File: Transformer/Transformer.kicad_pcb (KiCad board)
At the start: 4 copper layers, 36 x 30 mm, 0 parts

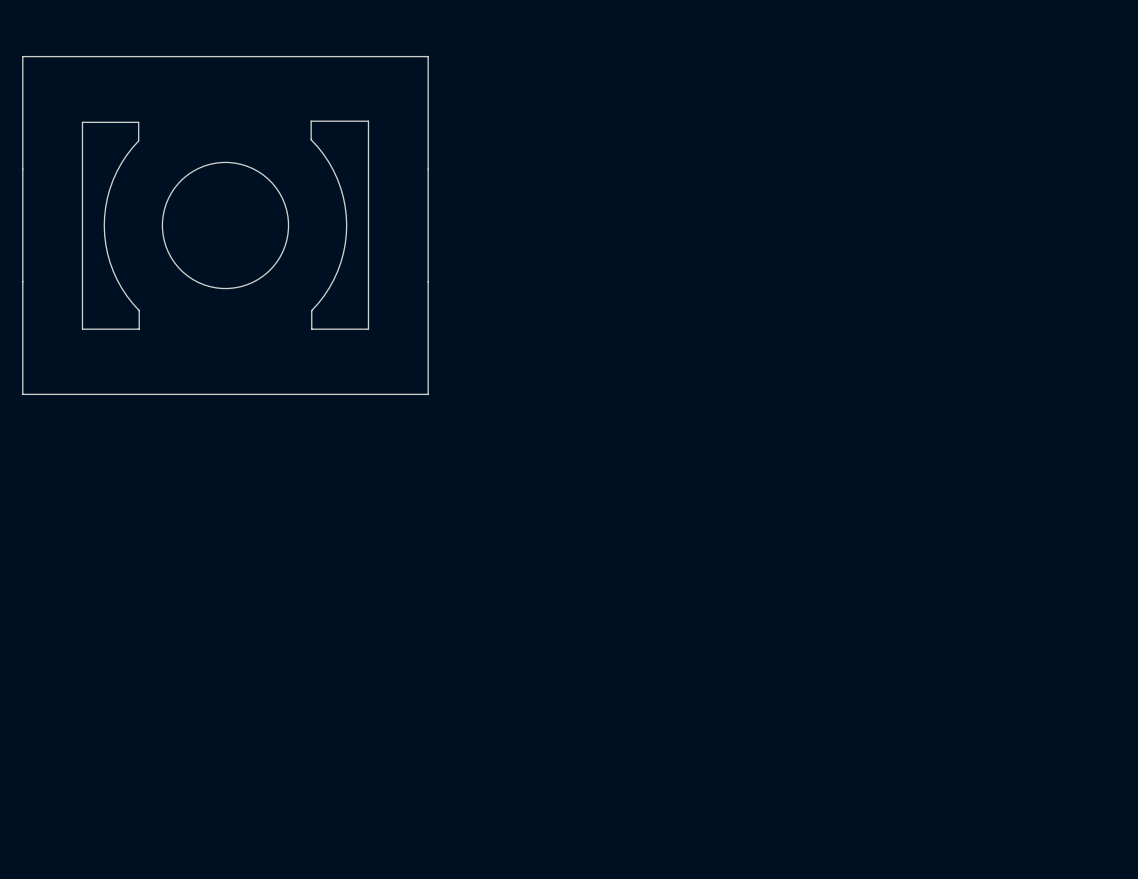
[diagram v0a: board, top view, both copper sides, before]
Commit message: Updated transformer
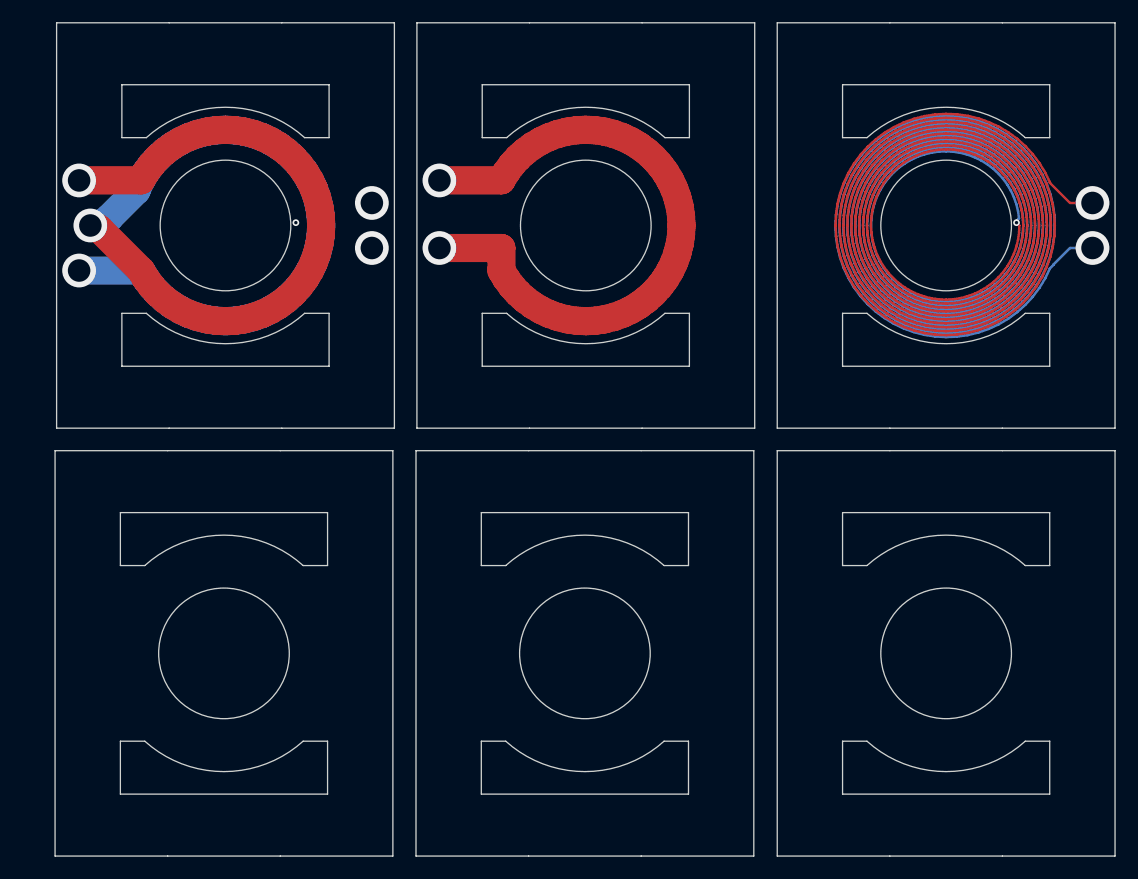
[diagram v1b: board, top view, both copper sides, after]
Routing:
- net (no net): track 0.00 -> 2247.1 mm, vias 0 -> 11
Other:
- board size 36 x 30 mm -> 94.1 x 74 mm

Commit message: Finished transformer
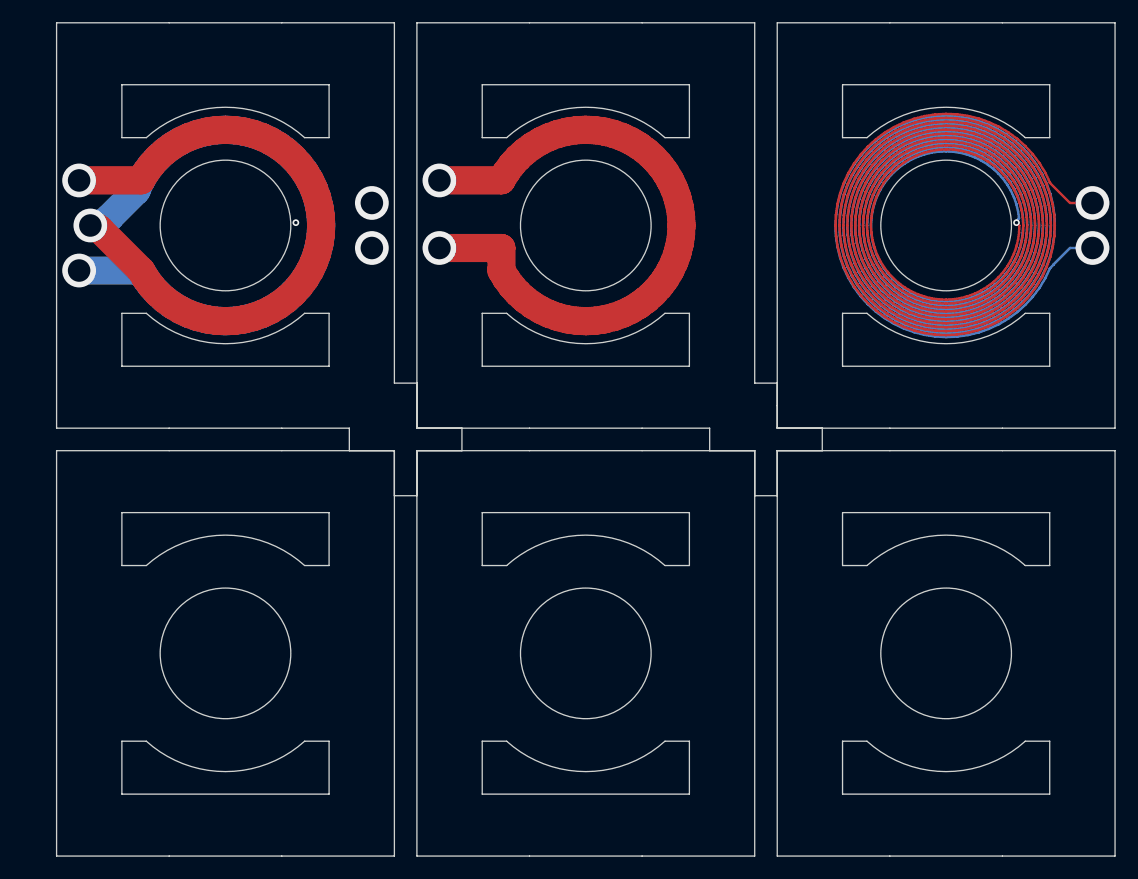
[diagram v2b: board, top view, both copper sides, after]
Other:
- board size 94.1 x 74 mm -> 94 x 74 mm

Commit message: Added vias to transformer blanks
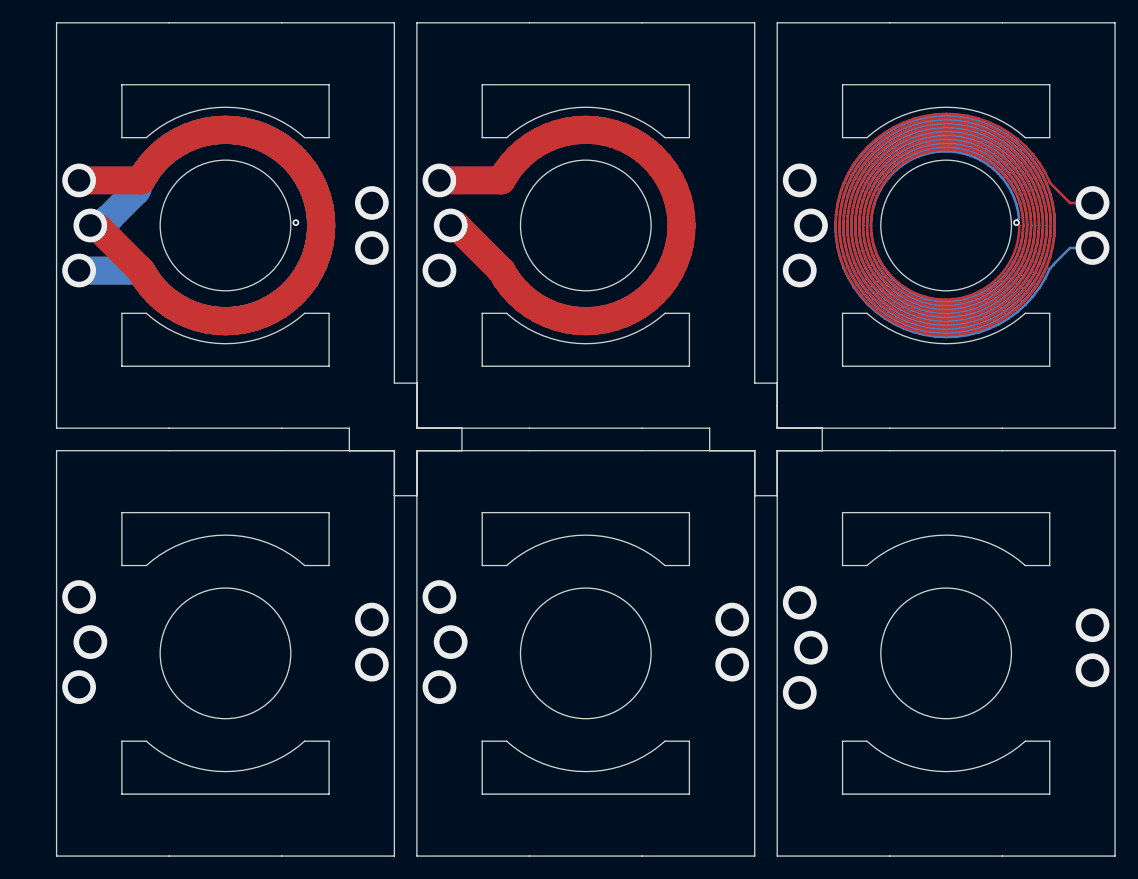
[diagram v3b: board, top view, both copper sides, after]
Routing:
- net (no net): track 2247.1 -> 2245.8 mm, vias 11 -> 30
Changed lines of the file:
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@@
 	)
 	(segment
+		(start 80.496797 63)
+		(end 80 63)
+		(width 2.5)
+		(layer "F.Cu")
+		(net "")
+	)
+	(segment
 		(start 129.931081 70.227043)
 		(end 129.197185 70.778138)
@@
 	)
 	(segment
+		(start 84.503669 67.006872)
+		(end 80.496797 63)
+		(width 2.5)
+		(layer "F.Cu")
+		(net "")
+	)
+	(segment
 		(start 130.297669 56.70233)
 		(end 130.888851 57.346465)
@@
 	)
 	(segment
-		(start 84.487076 65)
-		(end 79 65)
-		(width 2.5)
-		(layer "F.Cu")
-		(net "")
-	)
-	(segment
 		(start 117.828618 66.298672)
 		(end 117.529956 65.679979)
@@
 	)
 	(segment
-		(start 84.503669 65.016593)
-		(end 84.487076 65)
-		(width 2.5)
-		(layer "F.Cu")
-		(net "")
-	)
-	(segment
 		(start 117.628123 64.932887)
 		(end 117.463985 64.300094)
@@
 	)
 	(segment
-		(start 84.503669 67.006872)
-		(end 84.503669 65.016593)
-		(width 2.5)
-		(layer "F.Cu")
-		(net "")
-	)
-	(segment
 		(start 131.86908 58.793888)
 		(end 132.248511 59.583354)
@@
 	)
 	(via
+		(at 111 104.5)
+		(size 3)
+		(drill 2)
+		(layers "F.Cu" "B.Cu")
+		(net "")
+	)
+	(via
 		(at 137 61)
 		(size 3)
@@
 	)
 	(via
+		(at 137 98.5)
+		(size 3)
+		(drill 2)
+		(layers "F.Cu" "B.Cu")
+		(net "")
+	)
+	(via
+		(at 73 102)
+		(size 3)
+		(drill 2)
+		(layers "F.Cu" "B.Cu")
+		(net "")
+	)
+	(via
 		(at 79 59)
 		(size 3)
@@
 	)
 	(via
-		(at 79 65)
+		(at 105 98)
+		(size 3)
+		(drill 2)
+		(layers "F.Cu" "B.Cu")
+		(net "")
+	)
+	(via
+		(at 112 100.5)
+		(size 3)
+		(drill 2)
+		(layers "F.Cu" "B.Cu")
+		(net "")
+	)
+	(via
+		(at 80 63)
 		(size 3)
 		(drill 2)
@@
 	)
 	(via
+		(at 48 100)
+		(size 3)
+		(drill 2)
+		(layers "F.Cu" "B.Cu")
+		(net "")
+	)
+	(via
+		(at 111 96.5)
+		(size 3)
+		(drill 2)
+		(layers "F.Cu" "B.Cu")
+		(net "")
+	)
+	(via
 		(at 48 63)
 		(size 3)
@@
 	)
 	(via
+		(at 73 98)
+		(size 3)
+		(drill 2)
+		(layers "F.Cu" "B.Cu")
+		(net "")
+	)
+	(via
+		(at 47 96)
+		(size 3)
+		(drill 2)
+		(layers "F.Cu" "B.Cu")
+		(net "")
+	)
+	(via
+		(at 47 104)
+		(size 3)
+		(drill 2)
+		(layers "F.Cu" "B.Cu")
+		(net "")
+	)
+	(via
 		(at 73 61)
 		(size 3)
@@
 	)
 	(via
+		(at 79 67)
+		(size 3)
+		(drill 2)
+		(layers "F.Cu" "B.Cu")
+		(net "")
+	)
+	(via
+		(at 105 102)
+		(size 3)
+		(drill 2)
+		(layers "F.Cu" "B.Cu")
+		(net "")
+	)
+	(via
+		(at 111 67)
+		(size 3)
+		(drill 2)
+		(layers "F.Cu" "B.Cu")
+		(net "")
+	)
+	(via
+		(at 112 63)
+		(size 3)
+		(drill 2)
+		(layers "F.Cu" "B.Cu")
+		(net "")
+	)
+	(via
+		(at 111 59)
+		(size 3)
+		(drill 2)
+		(layers "F.Cu" "B.Cu")
+		(net "")
+	)
+	(via
 		(at 130.25 62.75)
 		(size 0.6)
@@
 	)
 	(via
+		(at 80 100)
+		(size 3)
+		(drill 2)
+		(layers "F.Cu" "B.Cu")
+		(net "")
+	)
+	(via
 		(at 47 59)
 		(size 3)
 		(drill 2)
+		(layers "F.Cu" "B.Cu")
+		(net "")
+	)
+	(via
+		(at 137 102.5)
+		(size 3)
+		(drill 2)
+		(layers "F.Cu" "B.Cu")
+		(net "")
+	)
+	(via
+		(at 79 96)
+		(size 3)
+		(drill 2)
+		(layers "F.Cu" "B.Cu")
+		(net "")
+	)
+	(via
+		(at 79 104)
+		(size 3)
+		(drill 2)

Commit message: Initial primary side layout
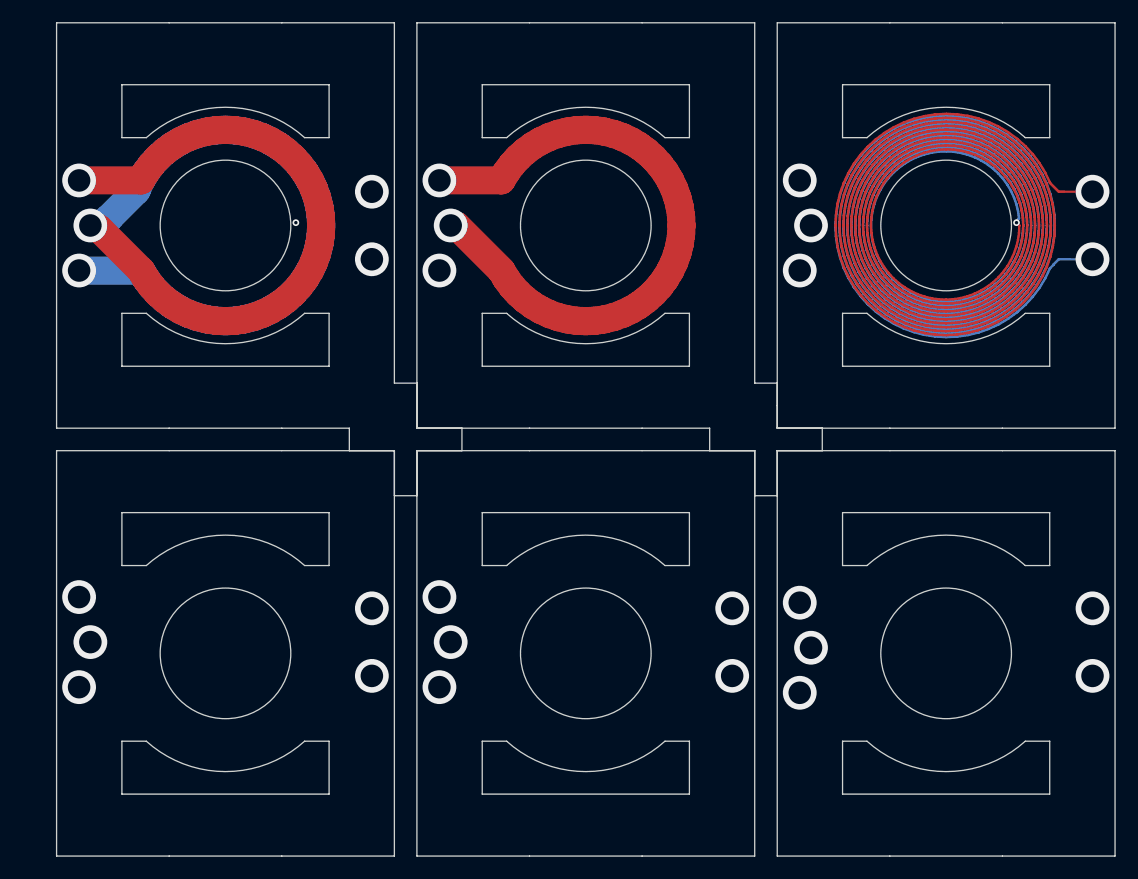
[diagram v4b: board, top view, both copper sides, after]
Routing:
- net (no net): track 2245.8 -> 2244.4 mm

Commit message: Fixed transformer boards
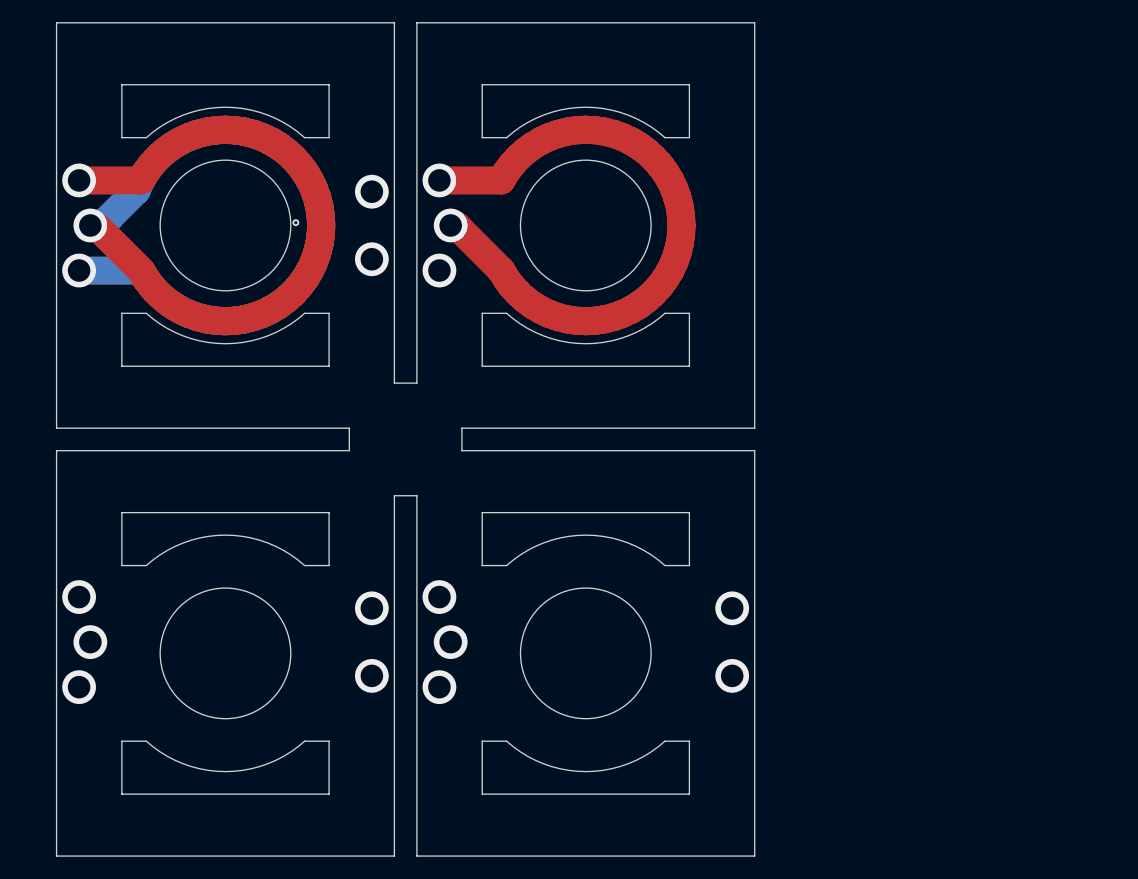
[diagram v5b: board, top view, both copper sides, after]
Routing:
- net (no net): track 2244.4 -> 1207.5 mm, vias 30 -> 19
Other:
- board size 94 x 74 mm -> 62 x 74 mm
